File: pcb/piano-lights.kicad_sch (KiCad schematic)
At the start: 36 parts, among them J1 FTDI RS232, J2 USB_B_Micro, J3 LED Strip, J4 AVR-ISP-6, J5 MIDI IN, J6 MIDI THRU, J7 MIDI Coupler Out, J8 MIDI Coupler In, SW1 Button, SW2 Reset, U1 ATmega328, U2 H11L1, U3 74AHC1G125, Y1 16MHz

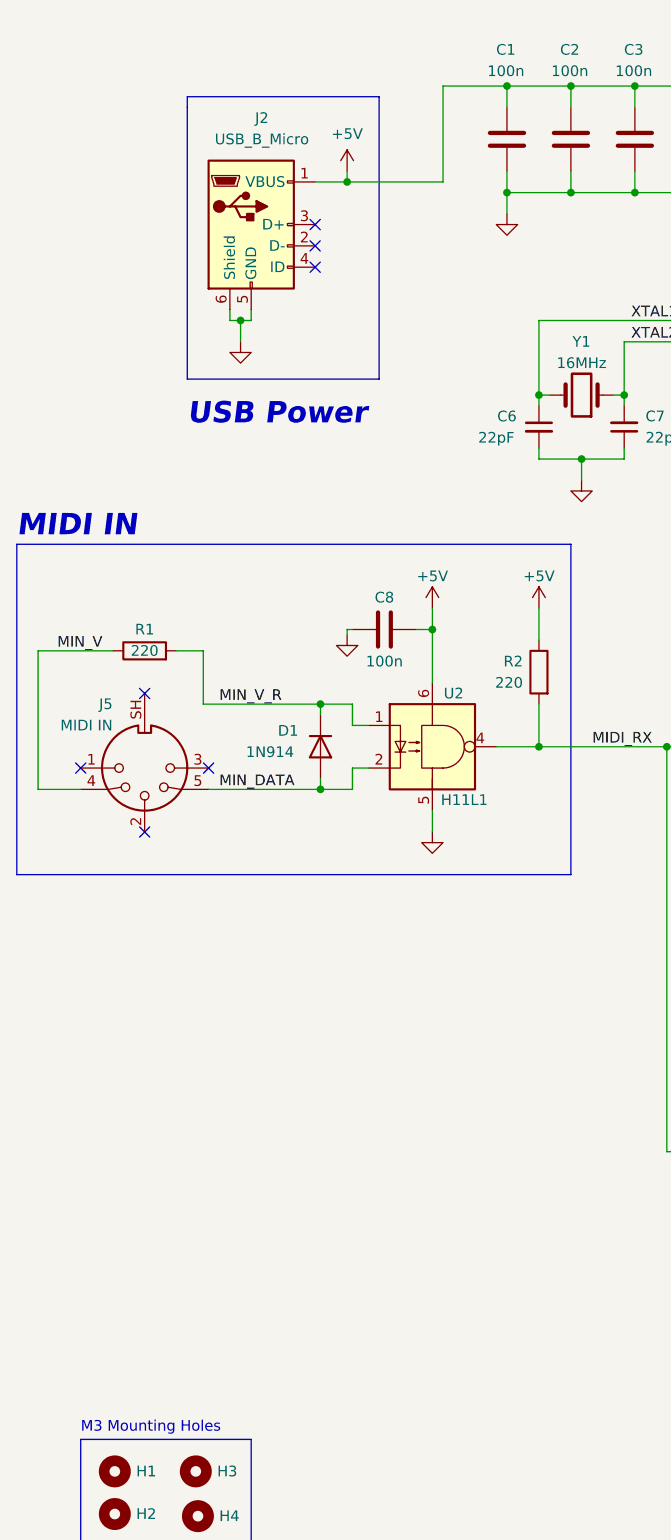
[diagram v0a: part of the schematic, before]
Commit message: Switch to USB-C 6-Pin for power on the schematic
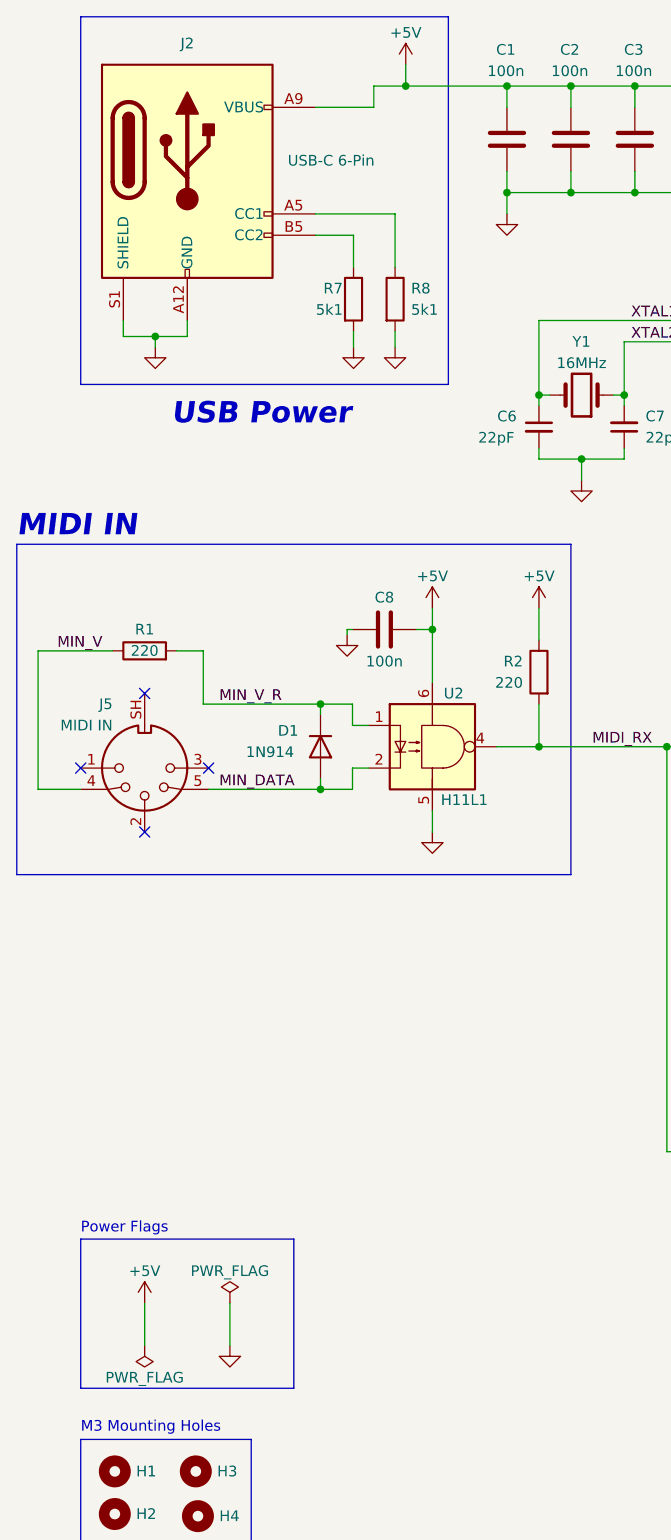
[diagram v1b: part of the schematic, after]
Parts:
- removed J2: USB_B_Micro, Connector_USB:USB_Micro-B_Wuerth_629105150521, symbol Connector:USB_B_Micro
- added J2: USB-C 6-Pin, 00-USB_C_GCT:GCT_USB4125-GF-A-0190_REVA2, symbol Connector:USB_C_Receptacle_PowerOnly_6P
- added R7, R8: 5k1, Resistor_SMD:R_0603_1608Metric_Pad0.98x0.95mm_HandSolder, symbol Device:R
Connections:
- net +5V: now also J2.A9 (VBUS), J2.B9 (VBUS)
- net GND: now also J2.A12 (GND), J2.B12 (GND), J2.S1 (SHIELD), R7.2, R8.2
- new net: J2.A5 (CC1), R8.1
- new net: J2.B5 (CC2), R7.1
- no-connect marks 29 -> 26
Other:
- note added: "Power Flags"

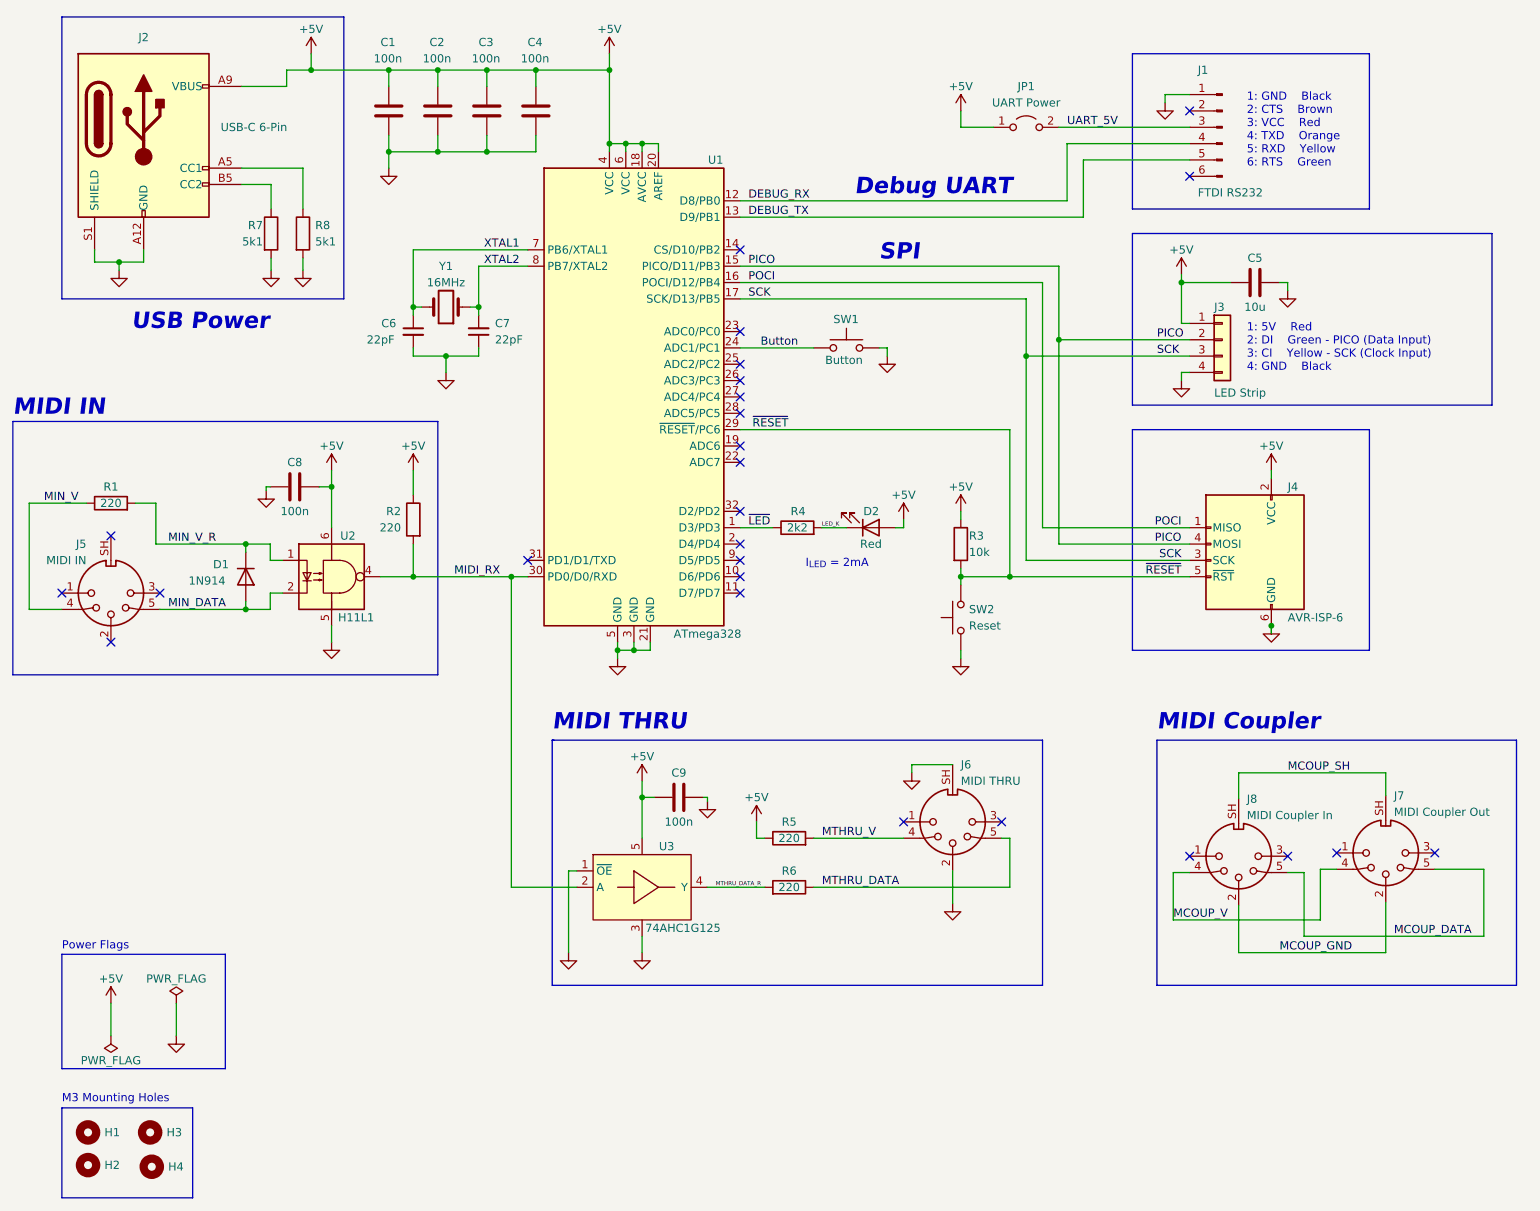
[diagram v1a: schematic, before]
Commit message: Start wiring up USB-C connector
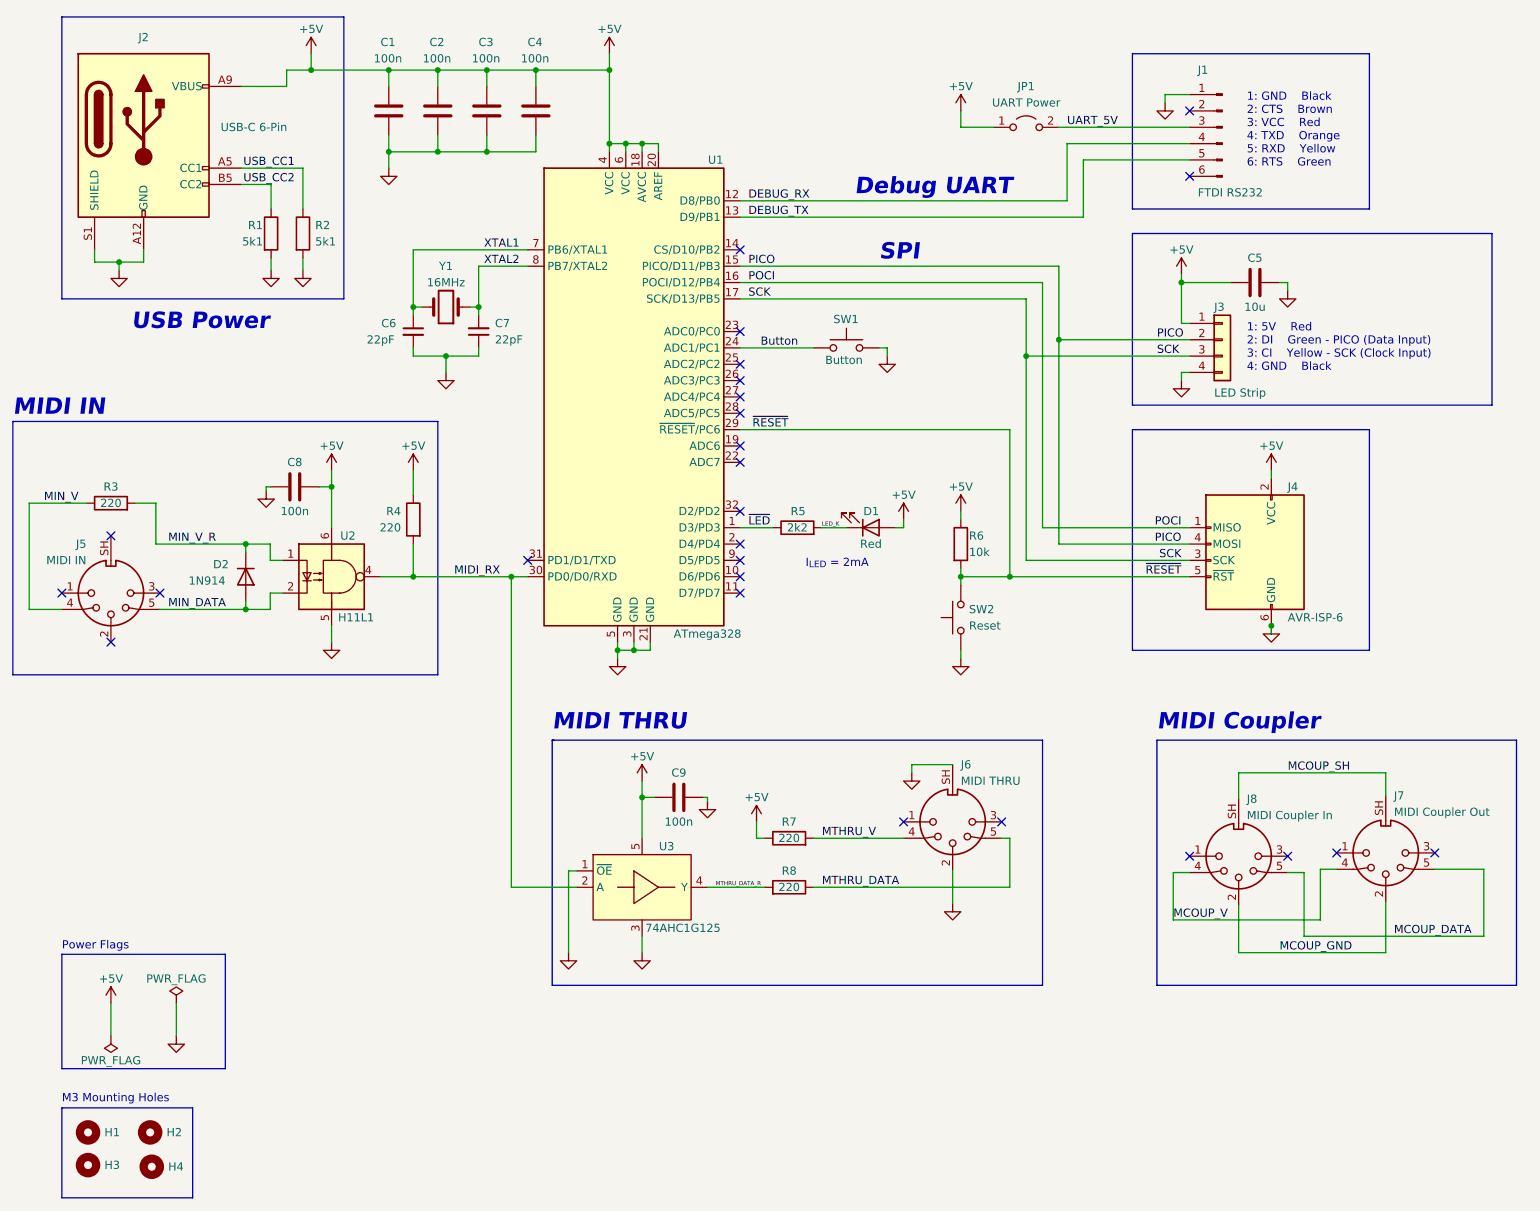
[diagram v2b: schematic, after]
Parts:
- renumbered D2 to D1, D1 to D2, H3 to H2, H2 to H3, R7 to R1, R8 to R2, R1 to R3, R2 to R4, R4 to R5, R3 to R6, R5 to R7, R6 to R8
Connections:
- net USB_CC1: now reaches J2.A5 (CC1), R2.1
- net USB_CC2: now reaches J2.B5 (CC2), R1.1

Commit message: Align some schematic components to 0.050in grid
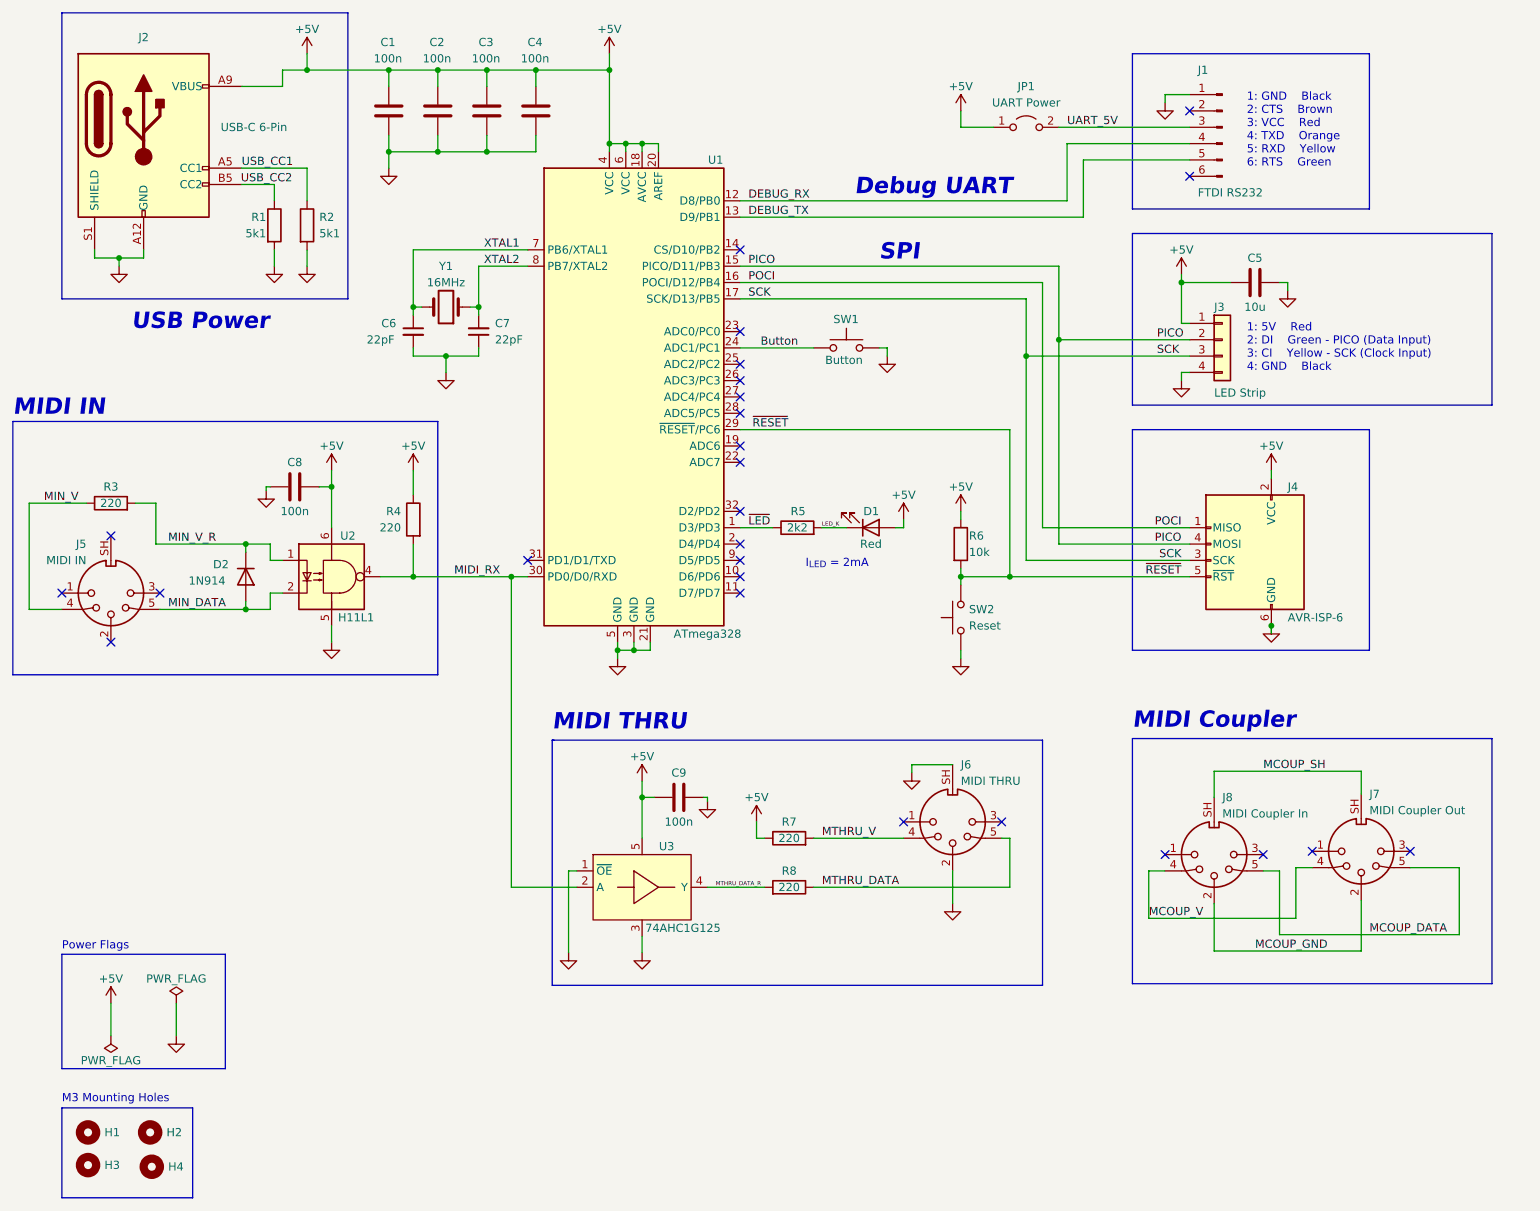
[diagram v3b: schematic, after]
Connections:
- net USB_CC2: no longer J2.B5 (CC2), R1.1
- new net: J2.B5 (CC2), R1.1
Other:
- moved on the sheet: J7, J8, R1, R2
